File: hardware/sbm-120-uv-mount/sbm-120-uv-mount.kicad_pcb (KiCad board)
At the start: 2 copper layers, 25 x 28 mm, 11 parts, among them J1 SpringConnector, J2 SpringConnector, J3 SpringConnector, J4 SpringConnector, J5 POWER_LED

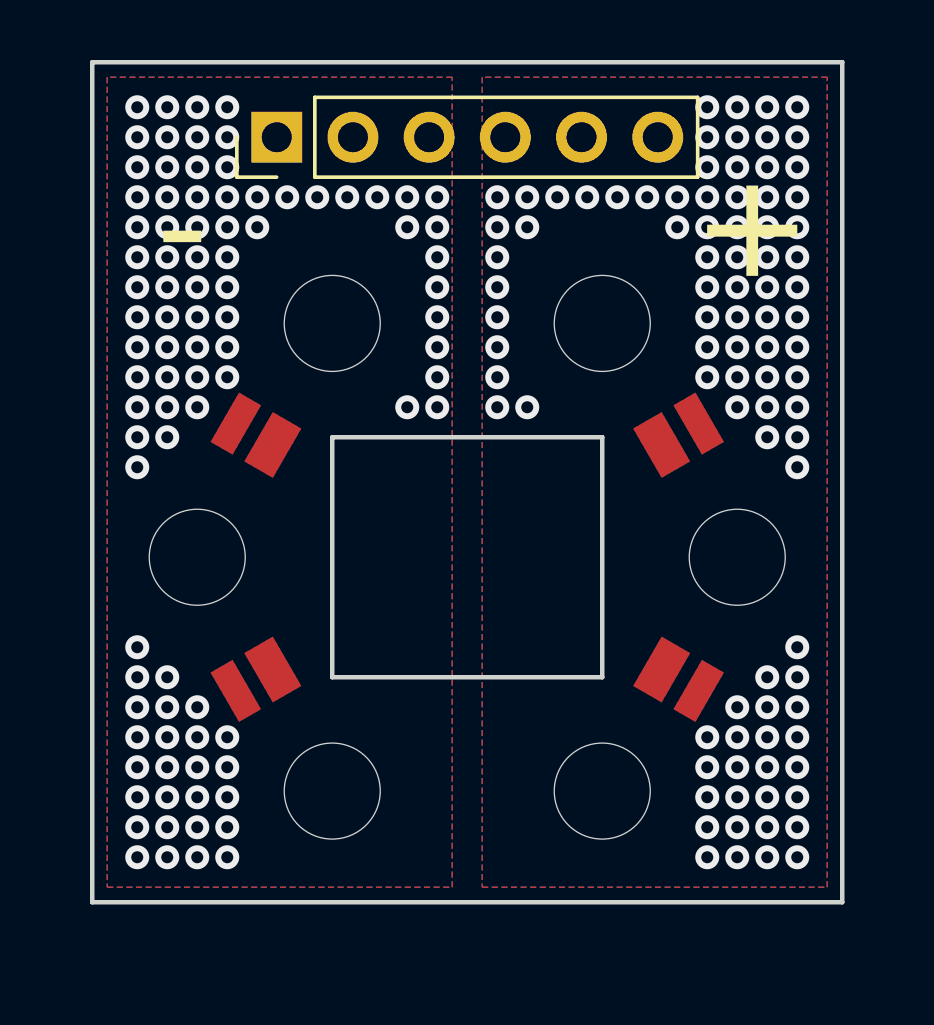
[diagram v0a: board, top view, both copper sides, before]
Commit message: with mounting holes, ready to order
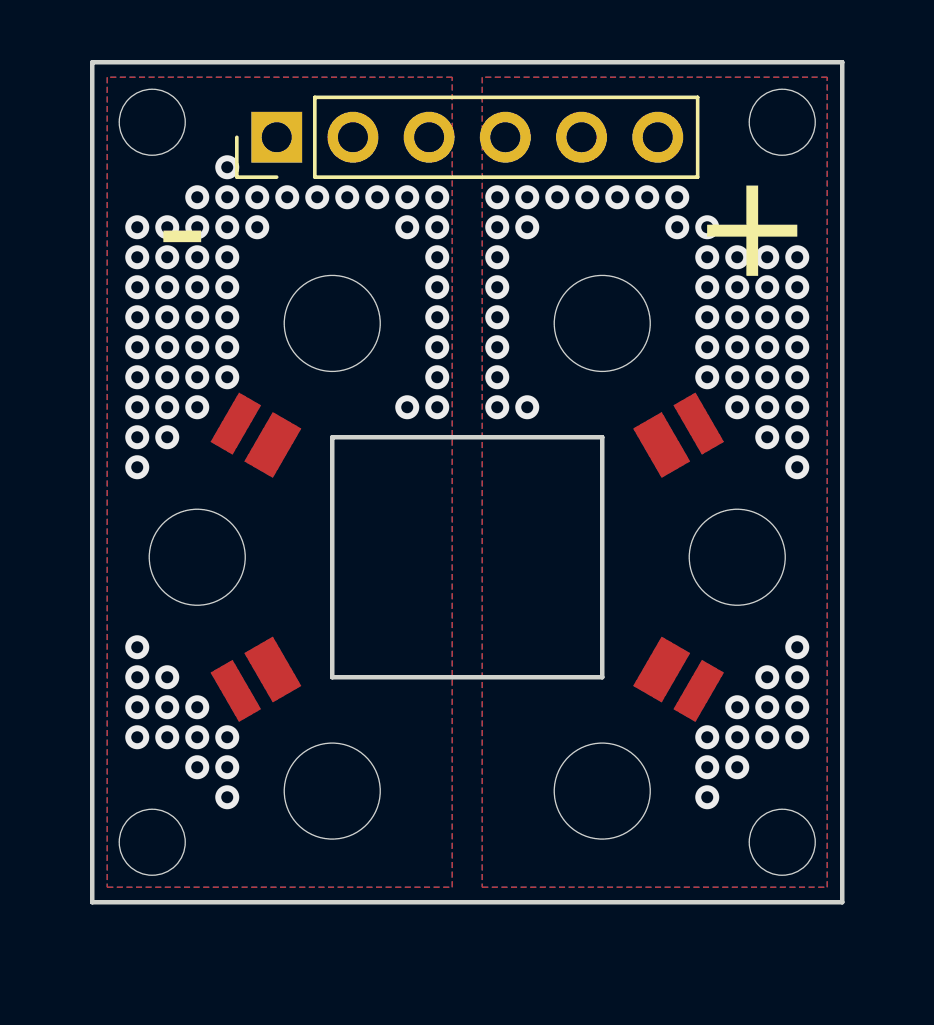
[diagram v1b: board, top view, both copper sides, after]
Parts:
- added H10: MountingHole, MountingHole:MountingHole_2.2mm_M2, F.Cu at (160.5, 109.5)
- added H7: MountingHole, MountingHole:MountingHole_2.2mm_M2, F.Cu at (160.5, 85.5)
- added H8: MountingHole, MountingHole:MountingHole_2.2mm_M2, F.Cu at (139.5, 109.5)
- added H9: MountingHole, MountingHole:MountingHole_2.2mm_M2, F.Cu at (139.5, 85.5)
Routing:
- net VEE: vias 89 -> 63
- net VDD: vias 89 -> 57
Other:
- rule pad_to_mask_clearance: 0.051 -> 0

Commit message: better
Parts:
- removed H1, H4: MountingHole, MountingHole:MountingHole_3.2mm_M3
- J1, J2, J3, J4: footprint custom_lib:TE-2286211-3 -> custom_lib:22862113
- moved H3 0.50 mm to (154.8, 91.8), turned to 240 degrees
- moved H2 0.50 mm to (145.2, 91.8), turned to 300 degrees
- moved H5 0.50 mm to (154.8, 108.2), turned to 300 degrees
- moved H6 0.50 mm to (145.2, 108.2), turned to 240 degrees
- moved J5 0.40 mm to (143.7, 85.6)
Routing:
- net VEE: vias 63 -> 88
- net VDD: vias 57 -> 88
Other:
- outline, holes or cut-outs redrawn

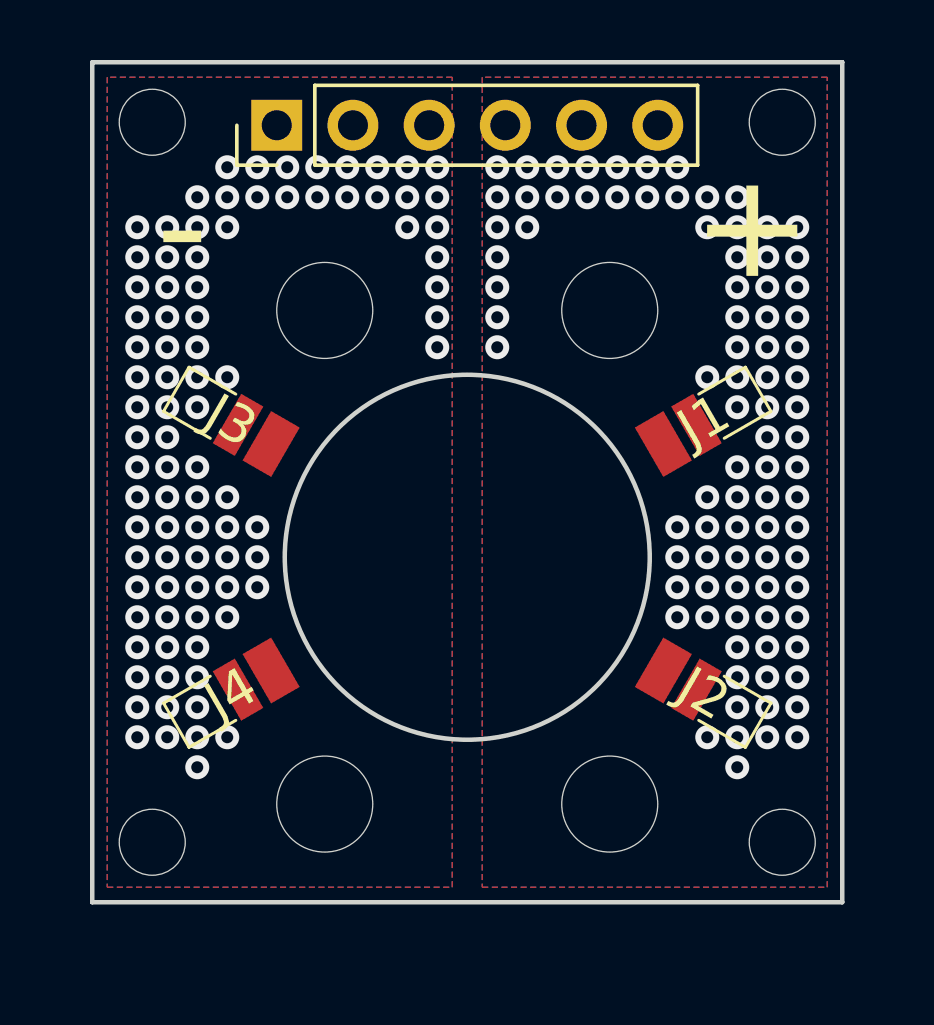
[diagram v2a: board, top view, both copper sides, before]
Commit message: smaller and square
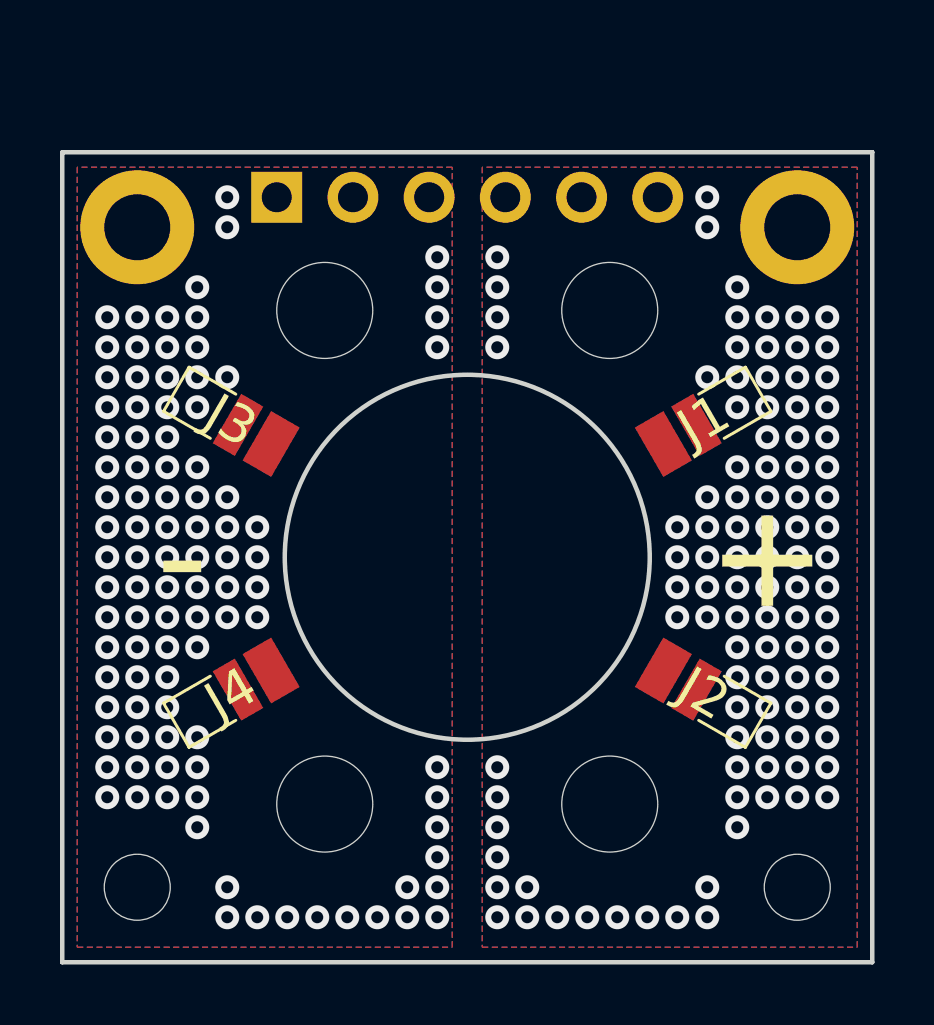
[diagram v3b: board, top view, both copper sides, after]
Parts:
- H7, H9: value MountingHole -> MountingHole_Pad; footprint MountingHole:MountingHole_2.2mm_M2 -> MountingHole:MountingHole_2.2mm_M2_DIN965_Pad
- J5: moved to B.Cu
- moved H7 3.54 mm to (161.0, 89.0)
- moved H9 3.54 mm to (139.0, 89.0)
- moved J5 2.40 mm to (143.7, 88.0), turned to 270 degrees
- moved H10 1.58 mm to (161.0, 111.0)
- moved H8 1.58 mm to (139.0, 111.0)
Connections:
- H7 pad 1: (no net) -> VDD
- H9 pad 1: (no net) -> VEE
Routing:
- net VEE: vias 88 -> 98
- net VDD: vias 88 -> 100
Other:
- board size 25 x 28 mm -> 27 x 27 mm
